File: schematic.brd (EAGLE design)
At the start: 160 x 100 mm, 89 parts, among them J1 MLX-2PIN, J10 JST-PA-4, J11 JST-PA-2, J12 JST-PA-2, J14 JST-PA-2, J15 JST-PA-2, J17 JST-PA-3, J18 JST-PA-3, J19 JST-PA-4, J2 MLX-2PIN, J20 JST-PA-4, J21 JST-PA-3, J22 JST-PA-3, J3 DF13-6, J4 DF13-5, J5 DF13-6, J6 SSW-116-02-S-TRA, J7 SSW-116-02-S-TRA, J8 SSW-108-02-S-D-RA, J9 SSW-106-02-S-D-RA, SW1 M2022LL2W13, SW2 M2022LL2W13, U1 VHE100W, U11 MED_MOSFET, U2 VHB150W, U4 INA139, U5 INA139, U6 INA139, U7 RELAY, U8 RELAY, U9 RELAY

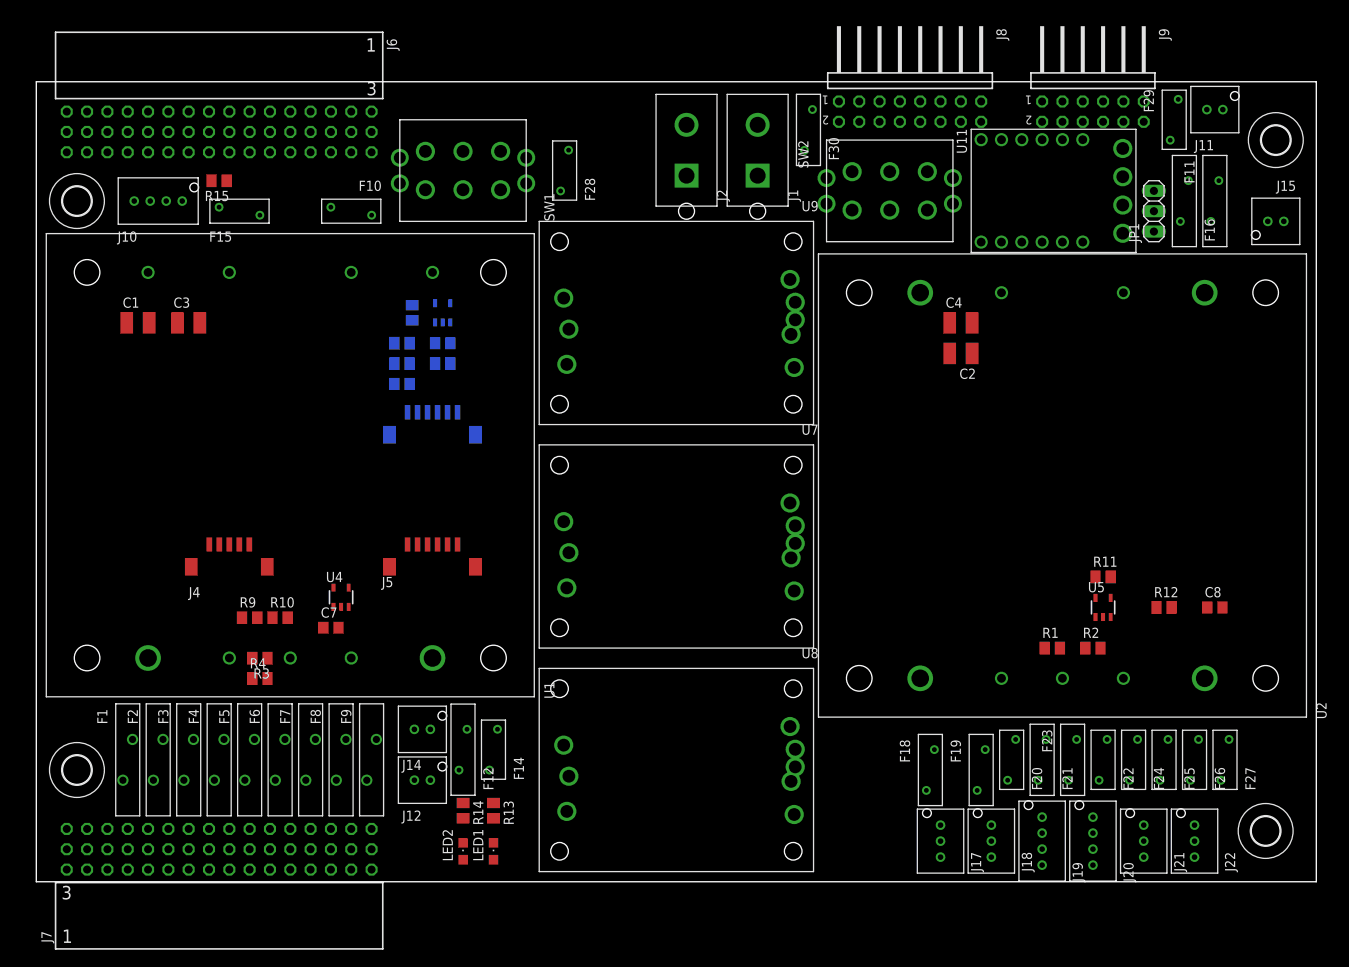
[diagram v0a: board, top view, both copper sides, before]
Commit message: Updating drawing with new right angle connectors on a single board side.
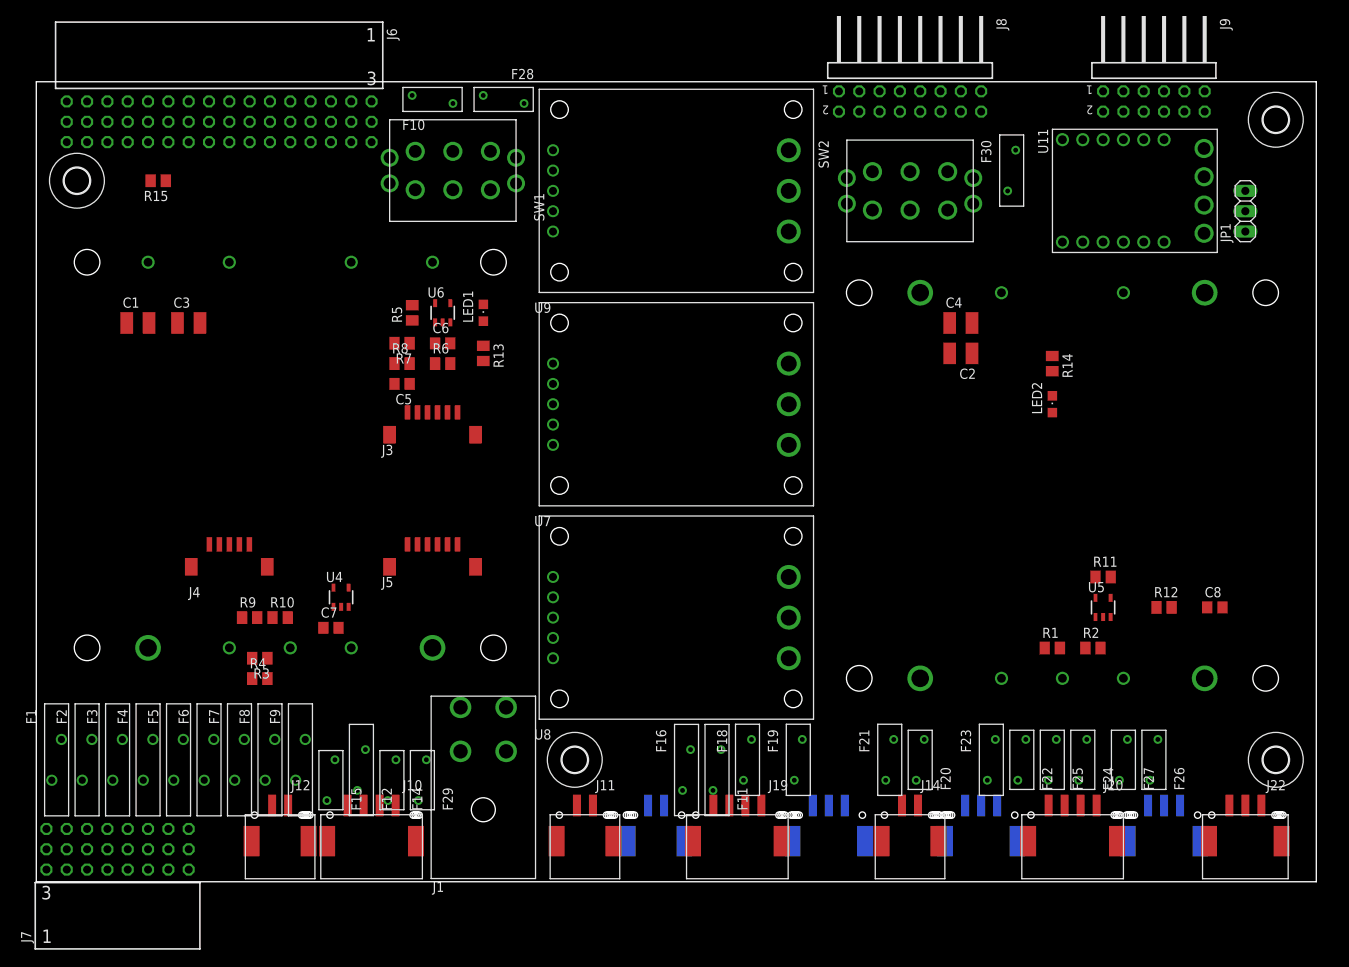
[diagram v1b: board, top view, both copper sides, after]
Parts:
- removed H1, H2, H3, H4: MOUNT-HOLE3.6, holes:3,6
- removed J2: MLX-2PIN, molex:2PIN
- added H5, H6, H7, H8: MOUNT-HOLE3.2, holes:3,2
- J1: value MLX-2PIN -> MEGAFIT-4SKT-RA; device molex:2PIN -> molex:MEGAFIT-4SKT-RA
- J10, J19, J20: value JST-PA-4 -> JST-PA-SMT-RA-4; device jst:JST-PA-4 -> jst:JST-PA-SMT-RA-4
- J11, J12, J14, J15: value JST-PA-2 -> JST-PA-SMT-RA-2; device jst:JST-PA-2 -> jst:JST-PA-SMT-RA-2
- J17, J18, J21, J22: value JST-PA-3 -> JST-PA-SMT-RA-3; device jst:JST-PA-3 -> jst:JST-PA-SMT-RA-3
- J7: value SSW-116-02-S-TRA -> SSW-108-02-S-TRA; device con-samtec:SSW-116-02-S-T-RA -> con-samtec:SSW-108-02-S-T-RA
- moved F29 125.1 mm to (48.3, 12.7), turned to 90 degrees
- moved J11 120.7 mm to (68.6, 5.08), turned to 180 degrees
- moved J15 109.6 mm to (77.5, 5.08), flipped to the bottom
- moved F11 94.5 mm to (85.1, 14.0), turned to 90 degrees
- moved F16 94.5 mm to (81.3, 14.0), turned to 270 degrees
- moved LED2 92.5 mm to (127.0, 59.7)
- moved R14 92.5 mm to (127.0, 64.8)
- moved J10 84.3 mm to (41.9, 5.08), turned to 180 degrees
- moved J1 80.1 mm to (55.9, 19.1), turned to 0 degrees
- moved F15 72.0 mm to (36.8, 12.7), turned to 90 degrees
- moved LED1 67.3 mm to (55.9, 71.1)
- moved J14 62.5 mm to (109.2, 5.08), turned to 180 degrees
- moved R13 57.2 mm to (55.9, 66.0)
- moved J19 38.1 mm to (87.6, 5.08), turned to 180 degrees
- moved F30 25.9 mm to (121.9, 88.9), turned to 270 degrees
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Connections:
- removed net N$24: J15.P2, U11.LGND
- removed net N$25: F16.P$2, J15.P1
- new net N$14: F16.P$2, J15.1
- new net N$16: J15.2, U11.LGND, U11.LGND2
- net AUX1: no longer J7.3
- net AUX2: no longer J7.6
- net AUX3: no longer J7.9
- net AUX4: no longer J7.12
- net AUX5: now also J10.3; no longer J10.P3, J7.15
- net AUX6: now also J10.2; no longer J10.P2, J7.18
- net FAUX_5V: no longer J7.11, J7.14, J7.17, J7.2, J7.44, J7.5, J7.8
- net FMAIN1_5V: now also J7.2; no longer J7.20
- net FMAIN2_5V: now also J7.5; no longer J7.23
- net FMAIN3_5V: now also J7.8; no longer J7.26
- net FMAIN4_5V: now also J7.11; no longer J7.29
- net FMAIN5_5V: now also J7.14; no longer J7.32
- net FMAIN6_5V: now also J7.17; no longer J7.35
- net FMAIN7_5V: now also J7.20; no longer J7.38
- net FMAIN8_5V: now also J7.23; no longer J7.41
- net GND: now also J10.4, J11.2, J12.2, J14.2, J17.2, J18.2, J19.3, J20.3, J21.3, J22.3; no longer J10.P4, J11.P2, J12.P2, J14.P2, J17.P2, J18.P2, J19.P3, J20.P3, J21.P3, J22.P3, J7.25, J7.28, J7.31, J7.34, J7.37, J7.40, J7.43, J7.46
- net MAIN1: now also J7.3; no longer J7.21
- net MAIN2: now also J7.6; no longer J7.24
- net MAIN3: now also J7.9; no longer J7.27
- net MAIN4: now also J7.12; no longer J7.30
- net MAIN5: now also J7.15; no longer J7.33
- net MAIN6: now also J7.18; no longer J7.36
- net MAIN7: now also J7.21; no longer J7.39
- net MAIN8: now also J7.24; no longer J7.42
- net N$1: now also J12.1; no longer J12.P1
- net N$10: now also J11.1; no longer J11.P1
- net N$12: now also J1.2; no longer J2.1
- net N$2: now also J10.1; no longer J10.P1
- net N$20: now also J14.1; no longer J14.P1
- net N$26: now also J19.1; no longer J19.P1
- net N$27: now also J19.2; no longer J19.P2
- net N$28: now also J20.1; no longer J20.P1
- net N$29: now also J20.2; no longer J20.P2
- net N$30: now also J17.1; no longer J17.P1
- net N$31: now also J18.1; no longer J18.P1
- net N$32: now also J22.2; no longer J22.P2
- net N$33: now also J22.1; no longer J22.P1
- net N$34: now also J21.2; no longer J21.P2
- net N$35: now also J21.1; no longer J21.P1
- net SBUS: no longer J7.45
- net SYNC: now also J17.3, J18.3, J19.4, J20.4; no longer J17.P3, J18.P3, J19.P4, J20.P4
- net V-: now also J1.3, J1.4; no longer J1.2, J2.2

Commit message: Adding some 5v ptc smt devices instead of the big throughhole units.
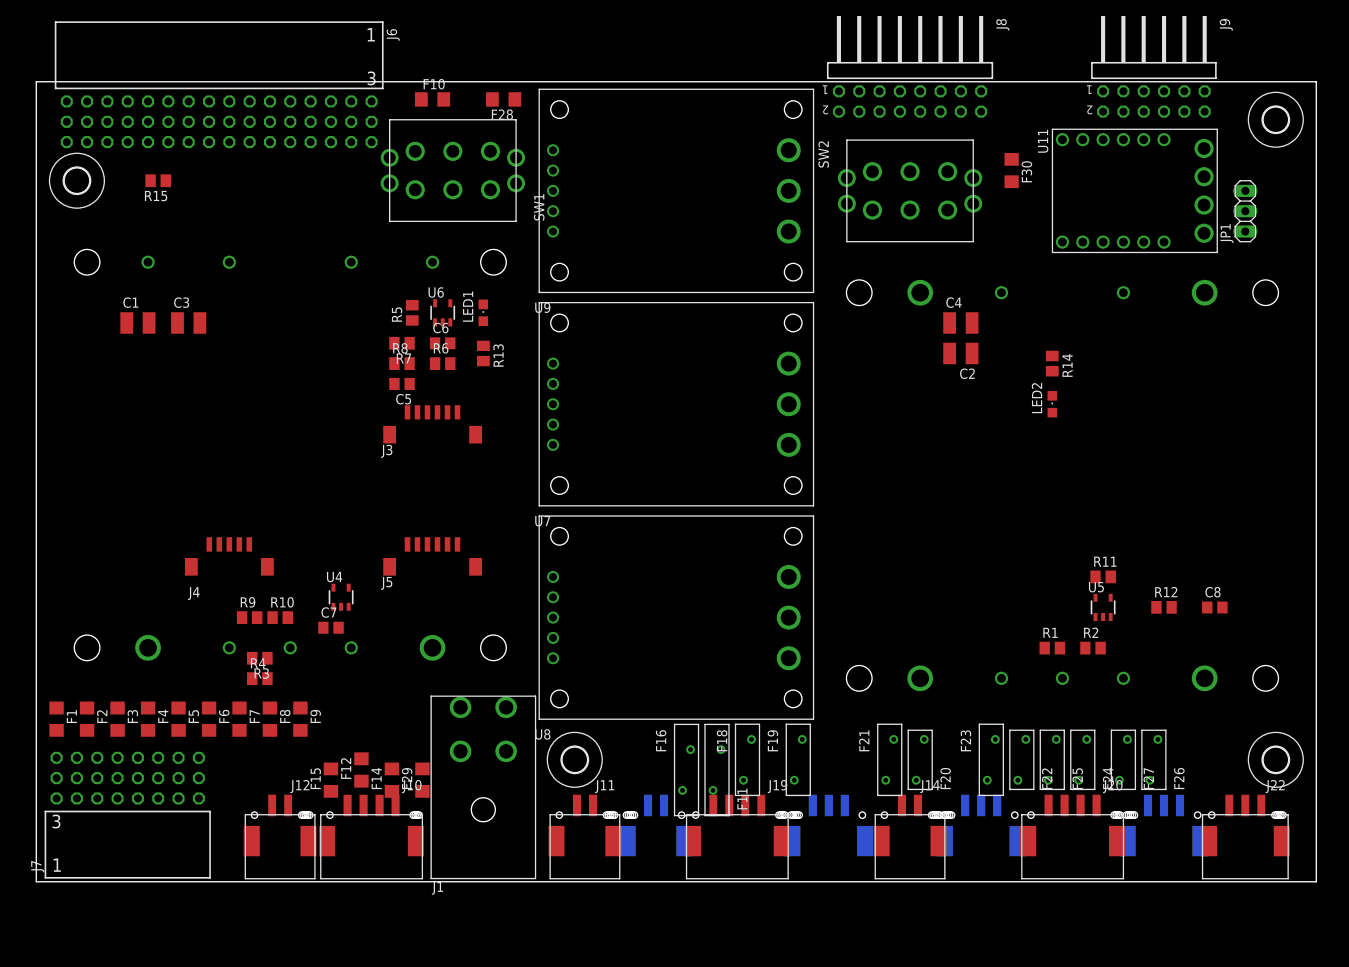
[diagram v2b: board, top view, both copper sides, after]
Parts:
- F1, F2, F3, F4, F5, F6, F7, F8, F9: value 30R400U -> 30R400ULORHO; device littelfuse:30R400U -> littelfuse:1206
- F10, F14, F15, F28, F29: value 30R110U -> 30R110ULORHO; device littelfuse:30R110U -> littelfuse:1206
- F12: value 30R250U -> 30R250ULORHO; device littelfuse:30R250U -> littelfuse:1206
- F30: value 30R160U -> 30R160ULORHO; device littelfuse:30R160U -> littelfuse:1206
- moved J7 8.98 mm to (11.4, 8.89)
- moved F1 5.08 mm to (2.54, 20.3)
- moved F2 5.08 mm to (6.35, 20.3)
- moved F3 5.08 mm to (10.2, 20.3)
- moved F4 5.08 mm to (14.0, 20.3)
- moved F5 5.08 mm to (17.8, 20.3)
- moved F6 5.08 mm to (21.6, 20.3)
- moved F7 5.08 mm to (25.4, 20.3)
- moved F8 5.08 mm to (29.2, 20.3)
- moved F9 5.08 mm to (33.0, 20.3)
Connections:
- net +5V: now also F1.1, F10.2, F12.2, F14.2, F15.2, F2.1, F28.2, F29.2, F3.1, F30.2, F4.1, F5.1, F6.1, F7.1, F8.1, F9.1; no longer F1.P$1, F10.P$2, F12.P$2, F14.P$2, F15.P$2, F2.P$1, F28.P$2, F29.P$2, F3.P$1, F30.P$2, F4.P$1, F5.P$1, F6.P$1, F7.P$1, F8.P$1, F9.P$1
- net FAUX_5V: now also F9.2; no longer F9.P$2
- net FMAIN1_5V: now also F1.2; no longer F1.P$2
- net FMAIN2_5V: now also F2.2; no longer F2.P$2
- net FMAIN3_5V: now also F3.2; no longer F3.P$2
- net FMAIN4_5V: now also F4.2; no longer F4.P$2
- net FMAIN5_5V: now also F5.2; no longer F5.P$2
- net FMAIN6_5V: now also F6.2; no longer F6.P$2
- net FMAIN7_5V: now also F7.2; no longer F7.P$2
- net FMAIN8_5V: now also F8.2; no longer F8.P$2
- net FRFD_5V: now also F30.1; no longer F30.P$1
- net N$1: now also F12.1; no longer F12.P$1
- net N$15: now also F28.1; no longer F28.P$1
- net N$2: now also F15.1; no longer F15.P$1
- net N$20: now also F14.1; no longer F14.P$1
- net N$3: now also F29.1; no longer F29.P$1
- net N$5: now also F10.1; no longer F10.P$1

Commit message: Updated so all fuses are SMT.
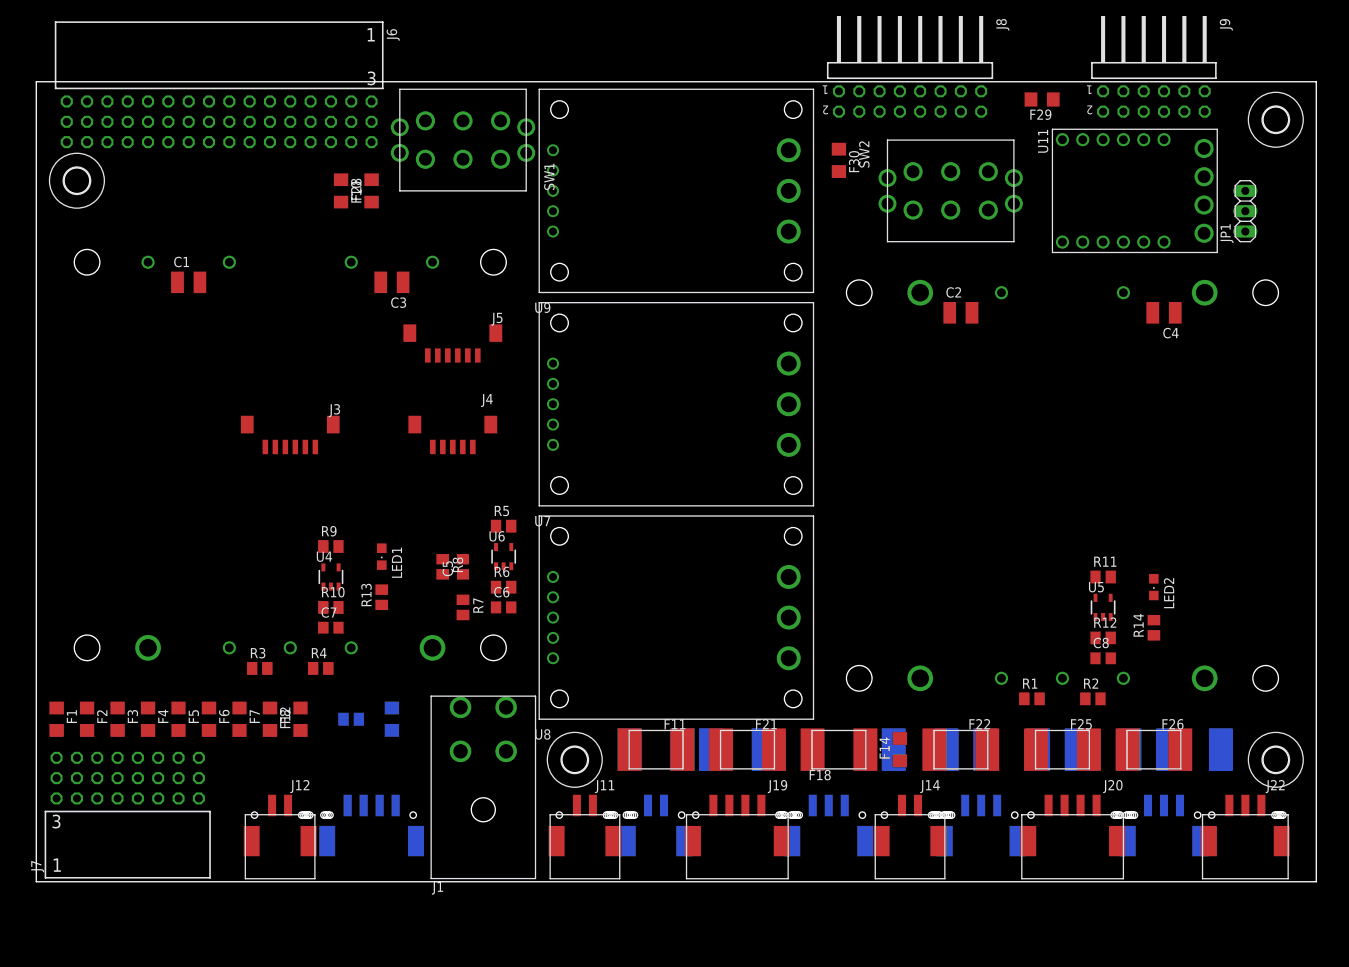
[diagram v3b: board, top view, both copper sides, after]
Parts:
- removed F9: 30R400ULORHO, littelfuse:1206
- F11: value 30R250U -> 30R110U2920L; device littelfuse:30R250U -> littelfuse:2920L
- F16: value 30R250U -> 30R250U2920L; device littelfuse:30R250U -> littelfuse:2920L
- F18, F19, F21, F23: value 30R160U -> 30R160U2920L; device littelfuse:30R160U -> littelfuse:2920L
- F20, F22, F24, F25, F26, F27: value 30R110U -> 30R110U2920L; device littelfuse:30R110U -> littelfuse:2920L
- moved F29 115.1 mm to (125.7, 97.8), turned to 180 degrees
- moved R15 71.5 mm to (39.4, 20.3), flipped to the bottom
- moved F14 63.6 mm to (108.0, 16.5)
- moved R14 35.4 mm to (139.7, 31.8), turned to 90 degrees
- moved C6 33.9 mm to (58.4, 34.3)
- moved R7 33.9 mm to (53.3, 34.3), turned to 270 degrees
- moved J4 33.1 mm to (52.1, 57.1), turned to 180 degrees
- moved LED1 33.0 mm to (43.2, 40.6), turned to 180 degrees
- moved R13 33.0 mm to (43.2, 35.6), turned to 90 degrees
- moved U6 31.4 mm to (58.4, 40.6)
- moved J5 29.3 mm to (52.1, 68.6), turned to 180 degrees
- moved R5 29.0 mm to (58.4, 44.5), turned to 0 degrees
- moved R6 29.0 mm to (58.4, 36.8)
- moved LED2 26.2 mm to (139.7, 36.8), turned to 180 degrees
- moved C3 25.9 mm to (44.5, 74.9), turned to 180 degrees
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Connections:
- removed net FAUX_5V: F9.2
- net +5V: no longer F9.1

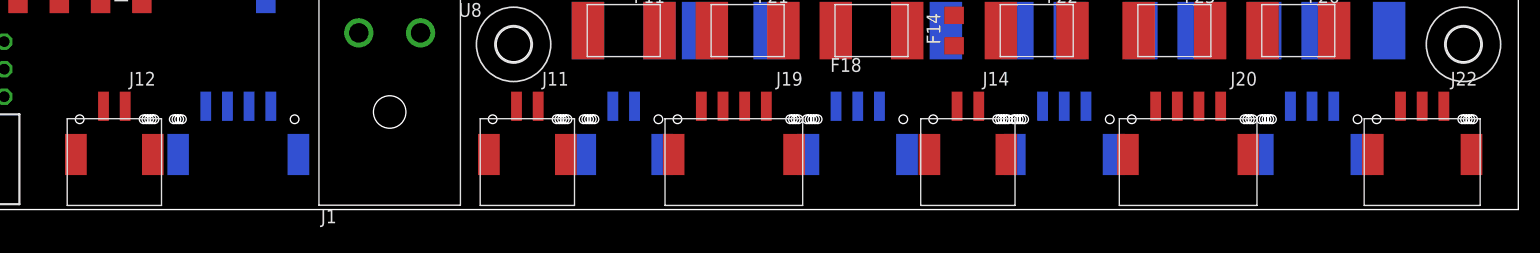
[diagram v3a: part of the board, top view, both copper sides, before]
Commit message: Basic text, pre autoroute.
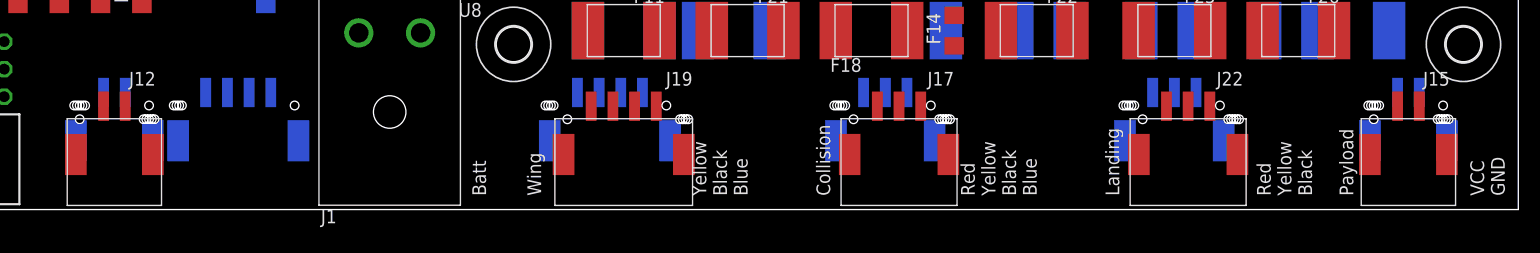
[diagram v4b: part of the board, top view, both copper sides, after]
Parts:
- moved J11 81.3 mm to (149.9, 6.35), flipped to the bottom
- moved J14 78.8 mm to (30.5, 6.35), flipped to the bottom
- moved J15 72.4 mm to (149.9, 5.08), flipped to the top
- moved J20 53.4 mm to (76.2, 6.35), flipped to the bottom
- moved J22 21.6 mm to (129.5, 5.08)
- moved J18 16.6 mm to (101.6, 6.35)
- moved J21 12.8 mm to (128.3, 6.35)
- moved J19 10.2 mm to (77.5, 5.08)
- moved J17 3.81 mm to (102.9, 5.08), flipped to the top
- moved J10 1.27 mm to (41.9, 6.35)
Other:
- board text added: "Batt"
- board text added: "Collision"
- board text added: "Landing"
- board text added: "Payload"
- board text added: "Red Yellow Black"
- board text added: "Red Yellow Black Blue"
- board text added: "VCC GND"
- board text added: "Wifi 24VDC"
- board text added: "Wing"
- board text added: "Yellow Black Blue"

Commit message: Power traces run, remainder are low current and can be autorouted.
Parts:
- R11, R5, R9: value (none) -> LVK25; device rcl:M0805 -> lvk_resistor:LVK25
- moved F14 72.4 mm to (35.6, 15.2)
- moved F11 62.2 mm to (139.7, 16.5), flipped to the bottom, turned to 0 degrees
- moved F16 62.2 mm to (139.7, 16.5), flipped to the top, turned to 0 degrees
- moved F22 38.1 mm to (77.5, 16.5), flipped to the bottom, turned to 0 degrees
- moved F23 34.3 mm to (87.6, 16.5), turned to 0 degrees
- moved C8 30.7 mm to (109.2, 47.0), turned to 180 degrees
- moved C7 29.0 mm to (14.0, 49.5), turned to 180 degrees
- moved R12 27.9 mm to (109.2, 44.5), turned to 180 degrees
- moved U5 26.2 mm to (108.0, 40.6), turned to 180 degrees
- moved R10 26.2 mm to (14.0, 47.0), turned to 180 degrees
- moved R11 25.7 mm to (108.0, 34.3)
- moved R9 24.7 mm to (12.7, 36.8)
- moved U4 24.7 mm to (12.7, 43.2), turned to 180 degrees
- moved F26 21.6 mm to (118.1, 16.5)
- moved LED2 20.4 mm to (119.4, 38.1)
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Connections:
- new net N$21: R1.1, R11.I2, U2.P8, U2.P9, U5.5
- new net N$22: R11.V1, U5.4
- new net N$23: R3.1, R9.I2, U1.P8, U1.P9, U4.5
- new net N$24: R5.V2, U6.3
- new net N$25: J1.1, J1.2, R5.I2, R7.2, U6.5
- new net N$36: R5.V1, U6.4
- net +24V: now also R11.I1; no longer R11.2, U5.4
- net +5V: now also R9.I1; no longer R9.2, U4.4
- net N$12: now also R9.V2, U4.3; no longer J1.1, J1.2, R5.1, R7.2, U6.3, U6.5
- net N$13: now also R9.V1, U4.4; no longer R3.1, R9.1, U1.P8, U1.P9, U4.3, U4.5
- net N$17: now also R11.V2; no longer R1.1, R11.1, U2.P8, U2.P9, U5.5
- net V+: now also R5.I1; no longer R5.2, U6.4
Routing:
- net V-: track 0.00 -> 161.2 mm
- net +24V: track 0.00 -> 76.2 mm
- net GND: track 0.00 -> 47.3 mm
- net +5V: track 0.00 -> 41.3 mm
- net N$25: track 0.00 -> 21.5 mm
- net V+: track 0.00 -> 16.2 mm
- net N$21: track 0.00 -> 14.9 mm
- net FMAIN8_5V: track 0.00 -> 12.5 mm
- net N$1: track 0.00 -> 12.3 mm
- net FMAIN7_5V: track 0.00 -> 12.0 mm
- net FMAIN6_5V: track 0.00 -> 10.7 mm
- net FMAIN5_5V: track 0.00 -> 9.42 mm
- net FMAIN4_5V: track 0.00 -> 8.77 mm
- net FMAIN2_5V: track 0.00 -> 8.77 mm
- net FMAIN1_5V: track 0.00 -> 8.29 mm
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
